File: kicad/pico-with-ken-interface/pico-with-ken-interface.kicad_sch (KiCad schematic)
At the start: 7 parts, among them U1 Pico, U3 XDZ254-2-15-W-2.5-G1, U5 PM254-2-15-W-8.5

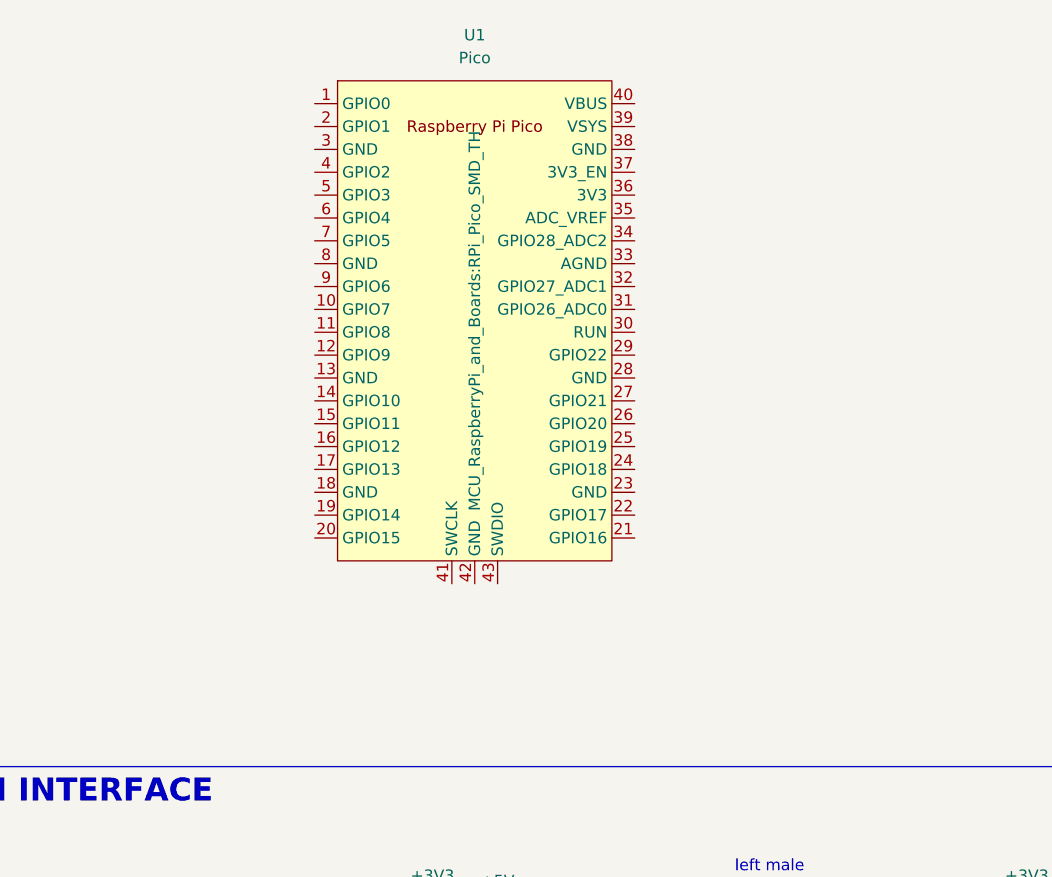
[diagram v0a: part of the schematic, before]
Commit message: bring back button symbol and foot print, did some routing.
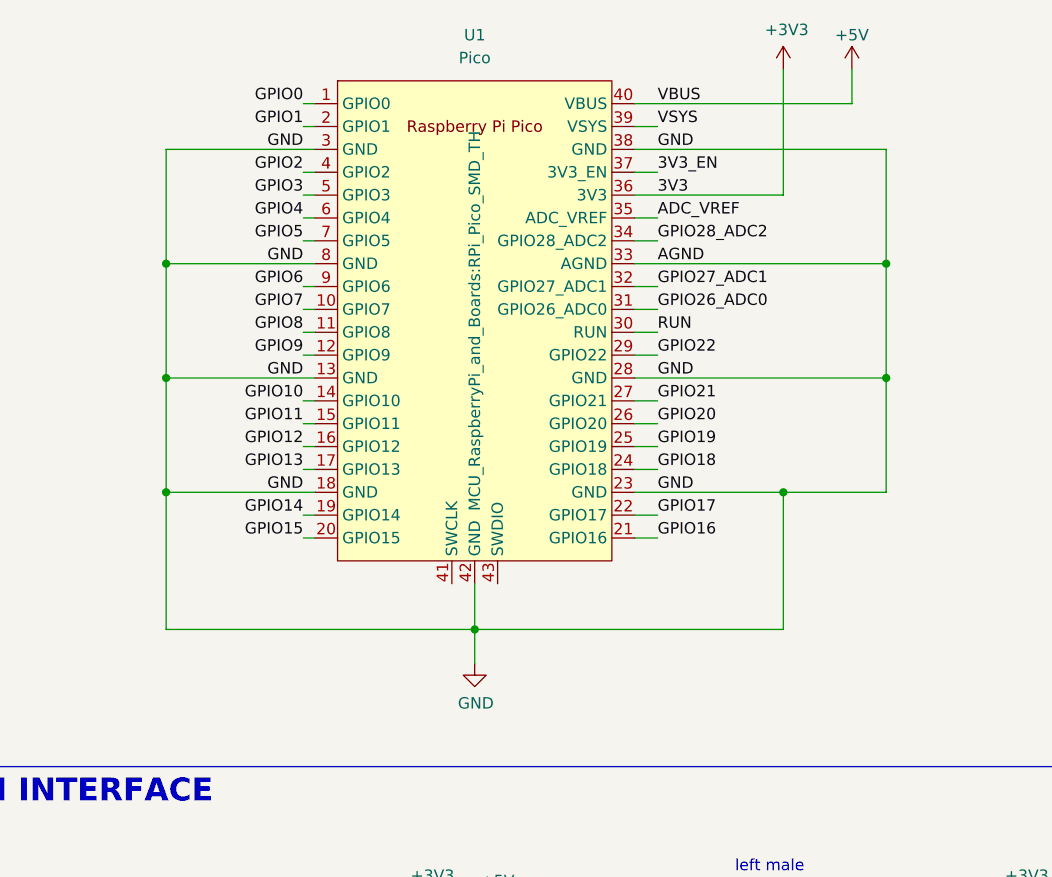
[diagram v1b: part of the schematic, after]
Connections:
- net +3V3: now also U1.36 (3V3)
- net +5V: now also U1.40 (VBUS)
- net GND: now also U1.13 (GND), U1.18 (GND), U1.23 (GND), U1.28 (GND), U1.3 (GND), U1.33 (AGND), U1.38 (GND), U1.42 (GND), U1.8 (GND)
- net GPIO0: now reaches U1.1 (GPIO0)
- net GPIO7: now reaches U1.10 (GPIO7)
- net GPIO8: now reaches U1.11 (GPIO8)
- net GPIO9: now reaches U1.12 (GPIO9)
- net GPIO10: now reaches U1.14 (GPIO10)
- net GPIO11: now reaches U1.15 (GPIO11)
- net GPIO12: now reaches U1.16 (GPIO12)
- net GPIO13: now reaches U1.17 (GPIO13)
- net GPIO14: now reaches U1.19 (GPIO14)
- net GPIO1: now reaches U1.2 (GPIO1)
- net GPIO15: now reaches U1.20 (GPIO15)
- net GPIO16: now reaches U1.21 (GPIO16)
- net GPIO17: now reaches U1.22 (GPIO17)
- net GPIO18: now reaches U1.24 (GPIO18)
- net GPIO19: now reaches U1.25 (GPIO19)
- net GPIO20: now reaches U1.26 (GPIO20)
- net GPIO21: now reaches U1.27 (GPIO21)
- net GPIO22: now reaches U1.29 (GPIO22)
- net RUN: now reaches U1.30 (RUN)
- net GPIO26_ADC0: now reaches U1.31 (GPIO26_ADC0)
- net GPIO27_ADC1: now reaches U1.32 (GPIO27_ADC1)
- net GPIO28_ADC2: now reaches U1.34 (GPIO28_ADC2)
- net ADC_VREF: now reaches U1.35 (ADC_VREF)
- net 3V3_EN: now reaches U1.37 (3V3_EN)
- net VSYS: now reaches U1.39 (VSYS)
- net GPIO2: now reaches U1.4 (GPIO2)
- net GPIO3: now reaches U1.5 (GPIO3)
- net GPIO4: now reaches U1.6 (GPIO4)
- net GPIO5: now reaches U1.7 (GPIO5)
- net GPIO6: now reaches U1.9 (GPIO6)

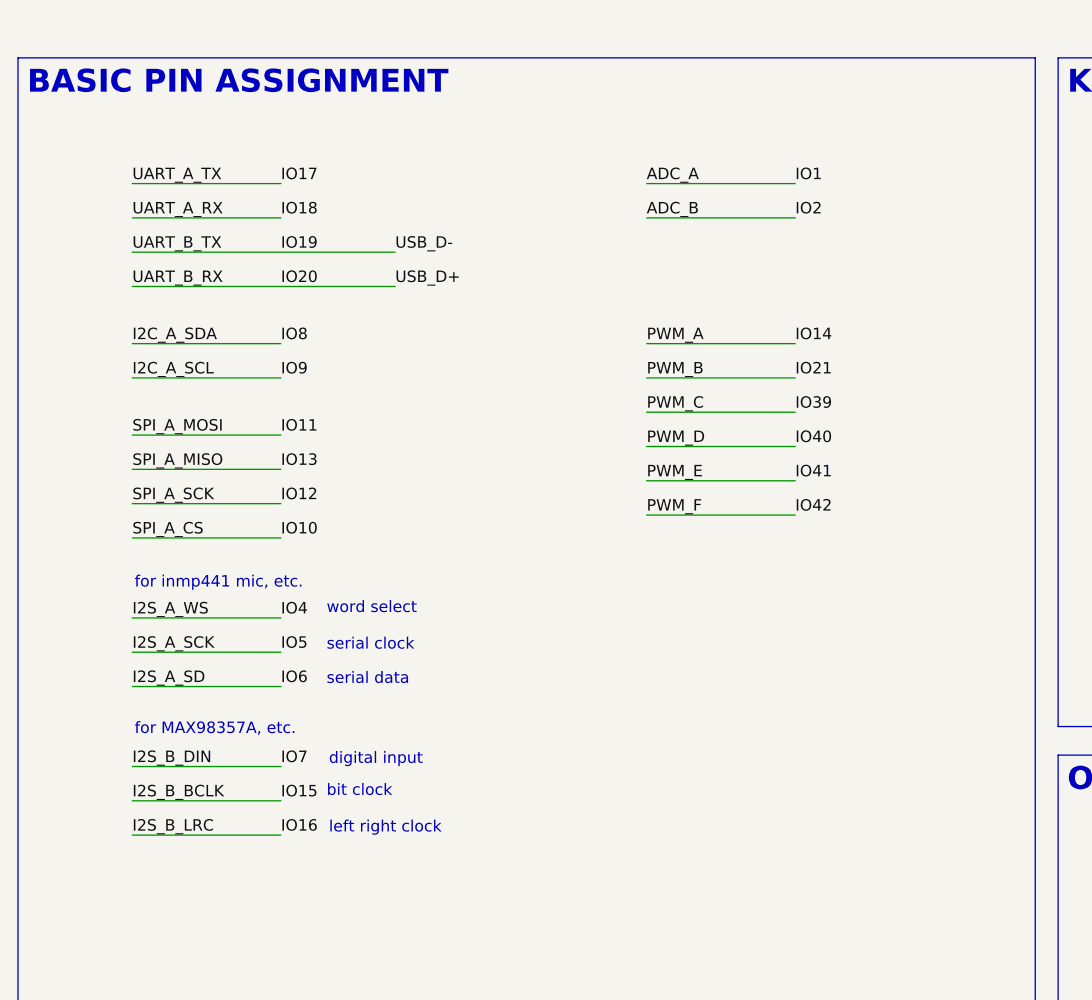
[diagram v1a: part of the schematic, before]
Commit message: first routing for pico
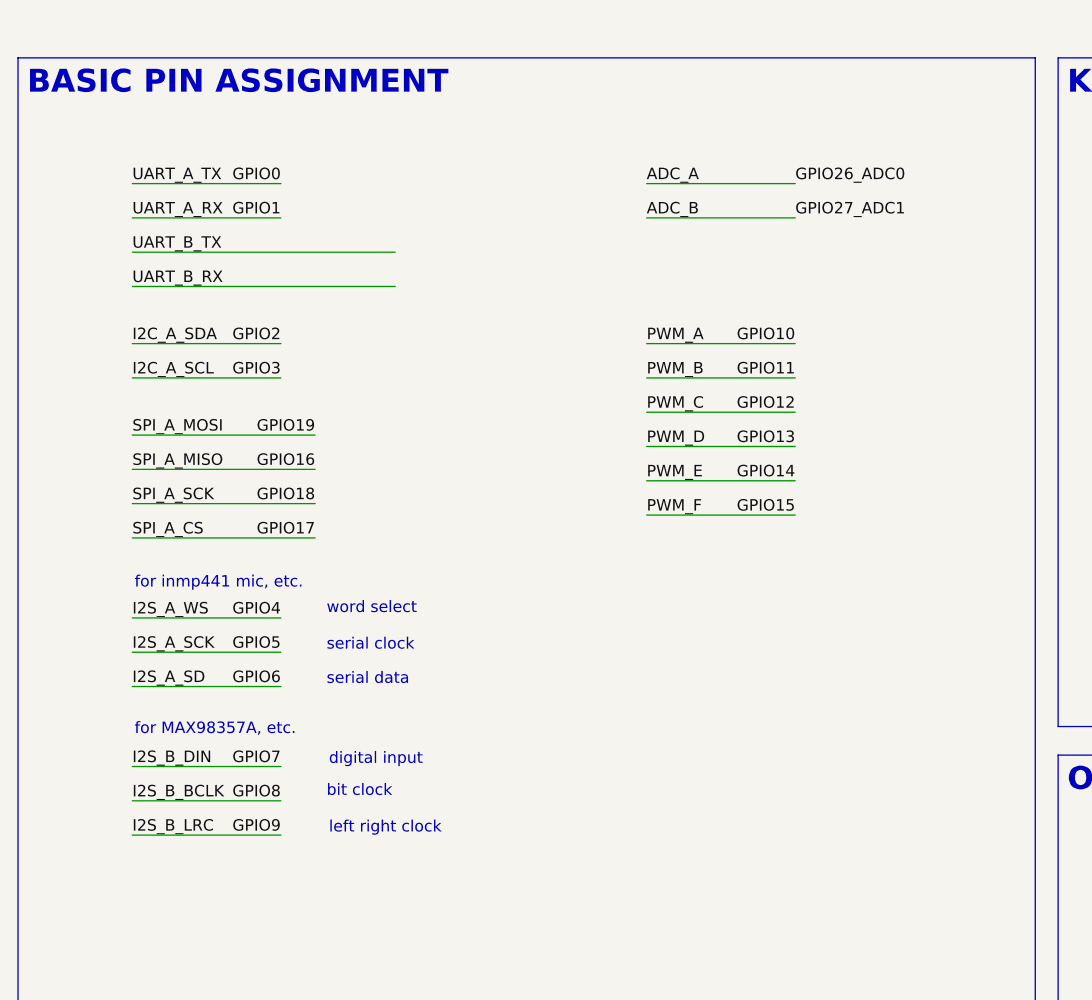
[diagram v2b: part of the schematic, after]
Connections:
- net GPIO26_ADC0 is gone; now on net ADC_A: U1.31 (GPIO26_ADC0)
- net GPIO27_ADC1 is gone; now on net ADC_B: U1.32 (GPIO27_ADC1)
- net I2C_A_SCL is gone; now on net GPIO3: U3.14, U5.18
- net I2C_A_SDA is gone; now on net GPIO2: U3.12, U5.20
- net I2S_A_SCK is gone; now on net GPIO5: U3.9, U5.21
- net I2S_A_SD is gone; now on net GPIO6: U3.11, U5.19
- net I2S_A_WS is gone; now on net GPIO4: U3.7, U5.23
- net I2S_B_BCLK is gone; now on net GPIO8: U3.17, U5.13
- net I2S_B_DIN is gone; now on net GPIO7: U3.15, U5.15
- net I2S_B_LRC is gone; now on net GPIO9: U3.19, U5.11
- net IO10 is gone; now on net GPIO17: U3.24, U5.8
- net IO11 is gone; now on net GPIO19: U3.18, U5.14
- net IO12 is gone; now on net GPIO18: U3.22, U5.10
- net IO13 is gone; now on net GPIO16: U3.20, U5.12
- net IO17 is gone; now on net GPIO0: U3.2, U5.30
- net IO18 is gone; now on net GPIO1: U3.4, U5.28
- net BTN_A: no longer U3.26, U5.6
- net BTN_B: no longer U3.28, U5.4
- net BTN_C: no longer U3.27, U5.3
- net BTN_D: no longer U3.29, U5.1
- net GPIO10: now also U3.26, U5.6
- net GPIO11: now also U3.28, U5.4
- net GPIO12: now also U3.27, U5.3
- net GPIO13: now also U3.29, U5.1
- net GPIO14: now also U3.23, U5.7
- net GPIO15: now also U3.25, U5.5
- net I2C_B_SCL: no longer U3.25, U5.5
- net I2C_B_SDA: no longer U3.23, U5.7
- net IO19 renamed UART_B_TX
- net IO20 renamed UART_B_RX

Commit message: add button and LED
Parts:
- added D3: LED, LED_SMD:LED_1206_3216Metric_Pad1.42x1.75mm_HandSolder, symbol Device:LED
- added R8: 1k, Resistor_SMD:R_0603_1608Metric_Pad0.98x0.95mm_HandSolder, symbol Device:R
- added SW2: TSC015A03526A, TSC015A03526A:SW-SMD_4P-L4.5-W4.5-P3.00-LS6.8, symbol TSC015A03526A:TSC015A03526A
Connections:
- net UART_B_RX is gone; now on net GPIO21: U3.8, U5.24
- net UART_B_TX is gone; now on net GPIO20: U3.6, U5.26
- net GND: now also D3.1 (K), SW2.3, SW2.4
- net GPIO22: now also SW2.2
- net GPIO28_ADC2: now also R8.1
- new net: D3.2 (A), R8.2
- no-connect marks 4 -> 5
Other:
- note added: "boot button"

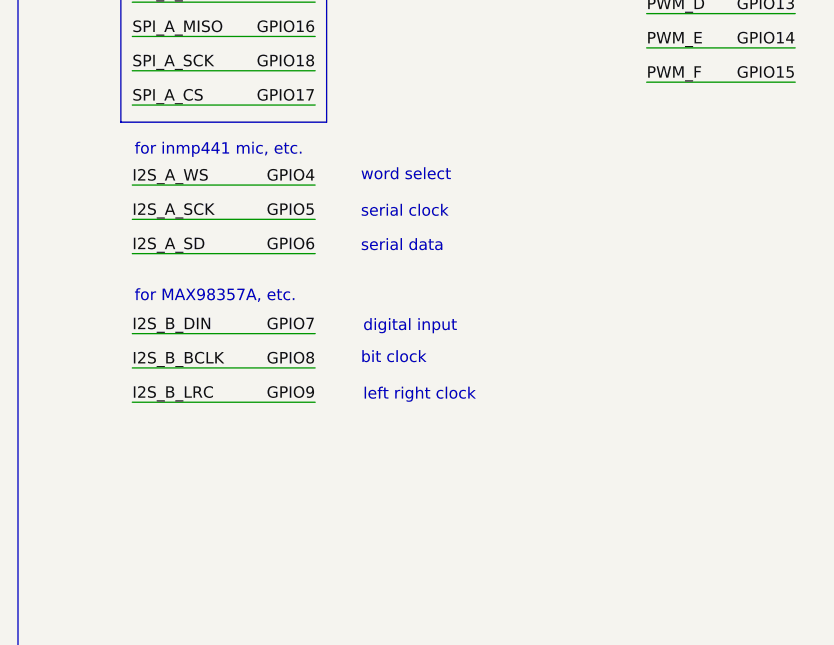
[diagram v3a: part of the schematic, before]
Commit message: finalize pin assignment for pico board
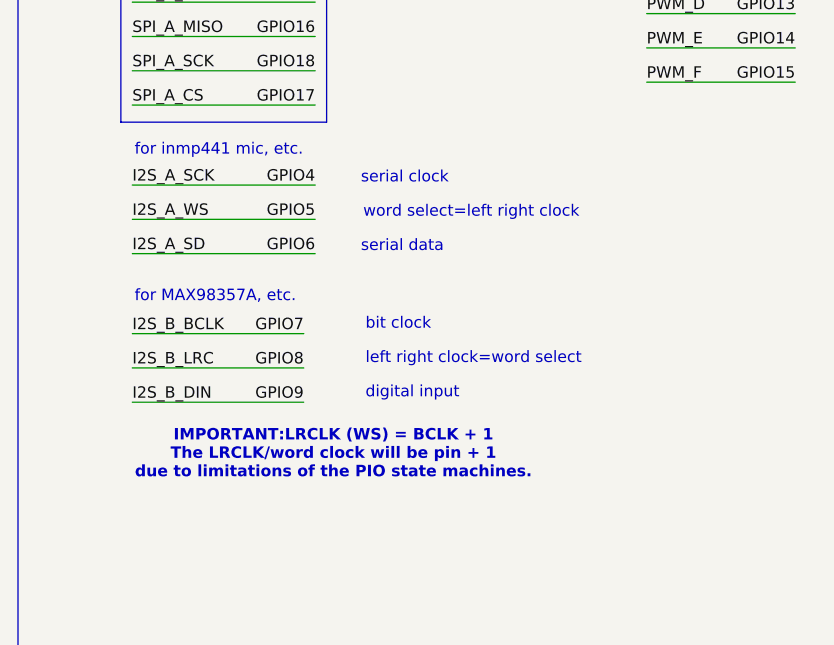
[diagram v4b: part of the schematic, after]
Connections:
- net GPIO4: now also U3.9, U5.21; no longer U3.7, U5.23
- net GPIO5: now also U3.7, U5.23; no longer U3.9, U5.21
- net GPIO7: now also U3.17, U5.13; no longer U3.15, U5.15
- net GPIO8: now also U3.19, U5.11; no longer U3.17, U5.13
- net GPIO9: now also U3.15, U5.15; no longer U3.19, U5.11
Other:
- note added: "IMPORTANT:LRCLK (WS) = BCLK + 1 The LRCLK/word clock will be pin + 1 due to limitations of the PIO state machines."
- note added: "left right clock=word select"
- note added: "word select=left right clock"
- note removed: "left right clock"
- note removed: "word select"

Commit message: use 4,5 for default I2C pins
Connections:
- net GPIO2: now also U3.9, U5.21; no longer U3.12, U5.20
- net GPIO3: now also U3.7, U5.23; no longer U3.14, U5.18
- net GPIO4: now also U3.12, U5.20; no longer U3.9, U5.21
- net GPIO5: now also U3.14, U5.18; no longer U3.7, U5.23
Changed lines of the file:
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@@
 	)
 	(rectangle
+		(start 26.67 157.48)
+		(end 53.34 165.1)
+		(stroke
+			(width 0)
+			(type default)
+		)
+		(fill
+			(type none)
+		)
+	)
+	(rectangle
 		(start 346.71 205.74)
 		(end 405.13 250.19)
@@
 		)
 	)
-	(label "GPIO2"
+	(label "GPIO4"
 		(at 52.07 160.02 180)
 		(effects
@@
 		)
 	)
-	(label "GPIO4"
+	(label "GPIO2"
 		(at 48.26 190.5 180)
 		(effects
@@
 		)
 	)
-	(label "GPIO3"
+	(label "GPIO5"
 		(at 52.07 163.83 180)
 		(effects
@@
 		)
 	)
-	(label "GPIO5"
+	(label "GPIO3"
 		(at 48.26 194.31 180)
 		(effects
